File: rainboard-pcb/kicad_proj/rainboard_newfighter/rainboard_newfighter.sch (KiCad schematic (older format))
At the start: 171 parts, among them J1 EJ508A, J2 C46390, J3 Conn_01x03, J4 Conn_01x03, J5 PH2-06-UA, J6 SDS-50J, J7 SDS-50J, J8 PH2-06-UA, J9 PH2-06-UA, Q1 DUAL 30V NMOS, Q2 DUAL 30V NMOS, Q3 30V 10mOhm, U1 RT8298, U2 ATmega16U2-MU, U4 74HC14, U5 ATmega16U2-MU, U6 ATmega2560-16AU, Y3 16MHz

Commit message: Minor schematic and library changes
Identical to previous commit, some files weren't saved.
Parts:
- gave numbers to parts that had none: 17
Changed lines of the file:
@@
 $EndComp
 $Comp
-L lib_symbol:C C?
+L lib_symbol:C C50
 U 1 1 601BBC3A
 P 25600 2900
-F 0 "C?" H 25625 3000 50  0000 L CNN
+F 0 "C50" H 25625 3000 50  0000 L CNN
 F 1 "1uF 25V" V 25450 2700 50  0000 L CNN
 F 2 "Capacitor_SMD:C_0805_2012Metric" H 25638 2750 50  0001 C CNN
@@
 $EndComp
 $Comp
-L lib_symbol:GND #PWR?
+L lib_symbol:GND #PWR0153
 U 1 1 601BBC44
 P 25600 3250
-F 0 "#PWR?" H 25600 3000 50  0001 C CNN
+F 0 "#PWR0153" H 25600 3000 50  0001 C CNN
 F 1 "GND" H 25600 3100 50  0000 C CNN
 F 2 "" H 25600 3250 50  0001 C CNN
@@
 5V_MCU
 $Comp
-L Device:R R?
+L Device:R R21
 U 1 1 605A86DB
 P 16750 5600
-F 0 "R?" H 16820 5646 50  0000 L CNN
+F 0 "R21" H 16820 5646 50  0000 L CNN
 F 1 "19.1k" H 16820 5555 50  0000 L CNN
 F 2 "Resistor_SMD:R_0603_1608Metric" V 16680 5600 50  0001 C CNN
@@
 	16750 6450 16750 6350
 $Comp
-L lib_symbol:GND #PWR?
+L lib_symbol:GND #PWR0154
 U 1 1 605A86E6
 P 16750 6450
-F 0 "#PWR?" H 16750 6200 50  0001 C CNN
+F 0 "#PWR0154" H 16750 6200 50  0001 C CNN
 F 1 "GND" H 16750 6300 50  0000 C CNN
 F 2 "" H 16750 6450 50  0001 C CNN
@@
 $EndComp
 $Comp
-L Device:C C?
+L Device:C C35
 U 1 1 605A86F1
 P 16750 6200
-F 0 "C?" H 16650 6050 50  0000 L CNN
+F 0 "C35" H 16650 6050 50  0000 L CNN
 F 1 "100nf" V 16900 6050 50  0000 L CNN
 F 2 "Capacitor_SMD:C_0603_1608Metric" H 16788 6050 50  0001 C CNN
@@
 	16750 5900 16750 6050
 $Comp
-L Device:C C?
+L Device:C C47
 U 1 1 606525C7
 P 23350 2150
-F 0 "C?" V 23500 1800 50  0000 L CNN
+F 0 "C47" V 23500 1800 50  0000 L CNN
 F 1 "100nf" V 23500 2000 50  0000 L CNN
 F 2 "Capacitor_SMD:C_0603_1608Metric" H 23388 2000 50  0001 C CNN
@@
 	21700 550  21700 8200
 $Comp
-L Device:Resonator Y?
+L Device:Resonator Y2
 U 1 1 60AB98BD
 P 21550 10250
-F 0 "Y?" V 21750 10000 50  0000 C CNN
+F 0 "Y2" V 21750 10000 50  0000 C CNN
 F 1 "16MHz" V 21850 10000 50  0000 C CNN
 F 2 "Crystal:Resonator_SMD_muRata_CSTxExxV-3Pin_3.0x1.1mm" H 21525 10250 50  0001 C CNN
@@
 	21300 10250 21350 10250
 $Comp
-L lib_symbol:GND #PWR?
+L lib_symbol:GND #PWR0157
 U 1 1 60BADC62
 P 16650 4200
-F 0 "#PWR?" H 16650 3950 50  0001 C CNN
+F 0 "#PWR0157" H 16650 3950 50  0001 C CNN
 F 1 "GND" H 16650 4050 50  0000 C CNN
 F 2 "" H 16650 4200 50  0001 C CNN
@@
 $EndComp
 $Comp
-L Device:Resonator Y?
+L Device:Resonator Y1
 U 1 1 60BADC6D
 P 16900 4200
-F 0 "Y?" V 17100 4100 50  0000 C CNN
+F 0 "Y1" V 17100 4100 50  0000 C CNN
 F 1 "16MHz" V 17200 4200 50  0000 C CNN
 F 2 "Crystal:Resonator_SMD_muRata_CSTxExxV-3Pin_3.0x1.1mm" H 16875 4200 50  0001 C CNN
@@
 	16650 4200 16700 4200
 $Comp
-L lib_symbol:C C?
+L lib_symbol:C C48
 U 1 1 60D193CE
 P 24750 9150
-F 0 "C?" H 24775 9250 50  0000 L CNN
+F 0 "C48" H 24775 9250 50  0000 L CNN
 F 1 "1uF 25V" V 24600 8950 50  0000 L CNN
 F 2 "Capacitor_SMD:C_0805_2012Metric" H 24788 9000 50  0001 C CNN
@@
 $EndComp
 $Comp
-L lib_symbol:GND #PWR?
+L lib_symbol:GND #PWR0188
 U 1 1 60D193D8
 P 24750 9500
-F 0 "#PWR?" H 24750 9250 50  0001 C CNN
+F 0 "#PWR0188" H 24750 9250 50  0001 C CNN
 F 1 "GND" H 24750 9350 50  0000 C CNN
 F 2 "" H 24750 9500 50  0001 C CNN
@@
 	24750 9500 24750 9300
 $Comp
-L Device:C C?
+L Device:C C49
 U 1 1 60D193E4
 P 25050 9150
-F 0 "C?" H 25200 9300 50  0000 L CNN
+F 0 "C49" H 25200 9300 50  0000 L CNN
 F 1 "100nf" V 25200 9000 50  0000 L CNN
 F 2 "Capacitor_SMD:C_0603_1608Metric" H 25088 9000 50  0001 C CNN
@@
 $EndComp
 $Comp
-L lib_symbol:GND #PWR?
+L lib_symbol:GND #PWR0189
 U 1 1 60D193EE
 P 25050 9500
-F 0 "#PWR?" H 25050 9250 50  0001 C CNN
+F 0 "#PWR0189" H 25050 9250 50  0001 C CNN
 F 1 "GND" H 25050 9350 50  0000 C CNN
 F 2 "" H 25050 9500 50  0001 C CNN
@@
 5V_USB
 $Comp
-L lib_symbol:C C?
+L lib_symbol:C C45
 U 1 1 60EF9A20
 P 20750 3450
-F 0 "C?" H 20775 3550 50  0000 L CNN
+F 0 "C45" H 20775 3550 50  0000 L CNN
 F 1 "1uF 25V" V 20600 3250 50  0000 L CNN
 F 2 "Capacitor_SMD:C_0805_2012Metric" H 20788 3300 50  0001 C CNN
@@
 $EndComp
 $Comp
-L lib_symbol:GND #PWR?
+L lib_symbol:GND #PWR0190
 U 1 1 60EF9A26
 P 20750 3800
-F 0 "#PWR?" H 20750 3550 50  0001 C CNN
+F 0 "#PWR0190" H 20750 3550 50  0001 C CNN
 F 1 "GND" H 20750 3650 50  0000 C CNN
 F 2 "" H 20750 3800 50  0001 C CNN
@@
 	20750 3800 20750 3600
 $Comp
-L Device:C C?
+L Device:C C46
 U 1 1 60EF9A2E
 P 21050 3450
-F 0 "C?" H 21200 3600 50  0000 L CNN
+F 0 "C46" H 21200 3600 50  0000 L CNN
 F 1 "100nf" V 21200 3300 50  0000 L CNN
 F 2 "Capacitor_SMD:C_0603_1608Metric" H 21088 3300 50  0001 C CNN
@@
 $EndComp
 $Comp
-L lib_symbol:GND #PWR?
+L lib_symbol:GND #PWR0191
 U 1 1 60EF9A34
 P 21050 3800
-F 0 "#PWR?" H 21050 3550 50  0001 C CNN
+F 0 "#PWR0191" H 21050 3550 50  0001 C CNN
 F 1 "GND" H 21050 3650 50  0000 C CNN
 F 2 "" H 21050 3800 50  0001 C CNN
@@
 	21050 3100 21050 3300
 $Comp
-L lib_symbol:C C?
+L lib_symbol:C C39
 U 1 1 60EF9A40
 P 19900 3450
-F 0 "C?" H 19925 3550 50  0000 L CNN
+F 0 "C39" H 19925 3550 50  0000 L CNN
 F 1 "1uF 25V" V 19750 3250 50  0000 L CNN
 F 2 "Capacitor_SMD:C_0805_2012Metric" H 19938 3300 50  0001 C CNN
@@
 $EndComp
 $Comp
-L lib_symbol:GND #PWR?
+L lib_symbol:GND #PWR0192
 U 1 1 60EF9A46
 P 19900 3800
-F 0 "#PWR?" H 19900 3550 50  0001 C CNN
+F 0 "#PWR0192" H 19900 3550 50  0001 C CNN
 F 1 "GND" H 19900 3650 50  0000 C CNN
 F 2 "" H 19900 3800 50  0001 C CNN
@@
 	19900 3800 19900 3600
 $Comp
-L Device:C C?
+L Device:C C41
 U 1 1 60EF9A4E
 P 20200 3450
-F 0 "C?" H 20350 3600 50  0000 L CNN
+F 0 "C41" H 20350 3600 50  0000 L CNN
 F 1 "100nf" V 20350 3300 50  0000 L CNN
 F 2 "Capacitor_SMD:C_0603_1608Metric" H 20238 3300 50  0001 C CNN
@@
 $EndComp
 $Comp
-L lib_symbol:GND #PWR?
+L lib_symbol:GND #PWR0193
 U 1 1 60EF9A54
 P 20200 3800
-F 0 "#PWR?" H 20200 3550 50  0001 C CNN
+F 0 "#PWR0193" H 20200 3550 50  0001 C CNN
 F 1 "GND" H 20200 3650 50  0000 C CNN
 F 2 "" H 20200 3800 50  0001 C CNN
@@
 Connection ~ 4800 10800
 $Comp
-L lib_symbol:C C?
+L lib_symbol:C C17
 U 1 1 6140F8CB
 P 3750 9550
-F 0 "C?" H 3775 9650 50  0000 L CNN
+F 0 "C17" H 3775 9650 50  0000 L CNN
 F 1 "1uF 25V" V 3600 9350 50  0000 L CNN
 F 2 "Capacitor_SMD:C_0805_2012Metric" H 3788 9400 50  0001 C CNN
@@
 $EndComp
 $Comp
-L lib_symbol:GND #PWR?
+L lib_symbol:GND #PWR0194
 U 1 1 6140F8D5
 P 3750 9900
-F 0 "#PWR?" H 3750 9650 50  0001 C CNN
+F 0 "#PWR0194" H 3750 9650 50  0001 C CNN
 F 1 "GND" H 3750 9750 50  0000 C CNN
 F 2 "" H 3750 9900 50  0001 C CNN
@@
 	3750 9200 3750 9400
 $Comp
-L lib_symbol:6N137 U?
+L lib_symbol:6N137 U3
 U 1 1 61517CC3
 P 3650 10600
-F 0 "U?" H 3490 10950 50  0000 C CNN
+F 0 "U3" H 3490 10950 50  0000 C CNN
 F 1 "6N137" H 3650 10250 50  0000 C CNN
 F 2 "" H 3650 10100 50  0001 C CNN
@@
 NONSTANDARD SO-8 PACKAGE
 $Comp
-L lib_symbol:C C?
+L lib_symbol:C C34
 U 1 1 61524583
 P 7350 12500
-F 0 "C?" H 7375 12600 50  0000 L CNN
+F 0 "C34" H 7375 12600 50  0000 L CNN
 F 1 "1uF 25V" V 7200 12300 50  0000 L CNN
 F 2 "Capacitor_SMD:C_0805_2012Metric" H 7388 12350 50  0001 C CNN
@@
 $EndComp
 $Comp
-L lib_symbol:C C?
+L lib_symbol:C C16
 U 1 1 615A0920
 P 1850 9900
-F 0 "C?" H 1875 10000 50  0000 L CNN
+F 0 "C16" H 1875 10000 50  0000 L CNN
 F 1 "DNP-1uF 25V" V 1700 9700 50  0000 L CNN
 F 2 "Capacitor_SMD:C_0805_2012Metric" H 1888 9750 50  0001 C CNN
@@
 $EndComp
 $Comp
-L lib_symbol:C C?
+L lib_symbol:C C4
 U 1 1 616161B4
 P 1500 11300
-F 0 "C?" H 1525 11400 50  0000 L CNN
+F 0 "C4" H 1525 11400 50  0000 L CNN
 F 1 "DNP-1uF 25V" V 1350 11100 50  0000 L CNN
 F 2 "Capacitor_SMD:C_0805_2012Metric" H 1538 11150 50  0001 C CNN
@@
 $EndComp
 $Comp
-L lib_symbol:GND #PWR?
+L lib_symbol:GND #PWR0195
 U 1 1 6168D233
 P 2150 9900
-F 0 "#PWR?" H 2150 9650 50  0001 C CNN
+F 0 "#PWR0195" H 2150 9650 50  0001 C CNN
 F 1 "GND" H 2150 9750 50  0000 C CNN
 F 2 "" H 2150 9900 50  0001 C CNN
@@
 $EndComp
 $Comp
-L lib_symbol:GND #PWR?
+L lib_symbol:GND #PWR0196
 U 1 1 617046B6
 P 1500 11600
-F 0 "#PWR?" H 1500 11350 50  0001 C CNN
+F 0 "#PWR0196" H 1500 11350 50  0001 C CNN
 F 1 "GND" H 1500 11450 50  0000 C CNN
 F 2 "" H 1500 11600 50  0001 C CNN

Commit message: Changes Micro USB to USB B
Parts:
- removed J2: C46390, symbol lib_symbol:USB_B_Micro
- added J2: USB_B, symbol lib_symbol:USB_B
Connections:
- net GND: now also J2.4 (GND)
- net at F2.2: now also J2.1 (VBUS)
- net at R7.2: now also J2.2 (D-)
- net at R6.2: now also J2.3 (D+)
- net at FB1.2: now also J2.5 (Shield)
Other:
- note added: "QUESTION, ASIDE FROM INPUT/OUTPUT CONNECTORS, WHAT ELSE NEEDS ESD PROTECTION?\nEVERY BUTTON/GPIO WOULD BE A LOT, MAYBE BEST TO JUST HAVE THE MCUs/ETC ON THE FAR SIDE SO USER CAN'T REACH MOST INPUTS"
- note added: "USB B Input"
- note removed: "Micro USB Input"
- note removed: "QUESTION, ASIDE FROM INPUT/OUTPUT CONNECTORS, WHAT ELSE NEEDS ESD PROTECTION?\nEVERY BUTTON/GPIO WOULD BE VERY MANY, MAYBE BEST TO JUST HAVE THE MCUs/ETC ON THE FAR SIDE SO USER CAN'T REACH MOST INPUTS"
- note removed: "QUESTION:\nMICRO OK, OR MINI?"
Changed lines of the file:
@@
 VLED
 Text Notes 500  3000 0    250  Italic 50
-Micro USB Input
-$Comp
-L lib_symbol:USB_B_Micro J2
-U 1 1 5FFD55EA
-P 1500 4050
-F 0 "J2" H 1300 4500 50  0000 L CNN
-F 1 "C46390" H 1300 4400 50  0000 L CNN
-F 2 "" H 1650 4000 50  0001 C CNN
-F 3 "~" H 1650 4000 50  0001 C CNN
-	1    1500 4050
-	1    0    0    -1
-$EndComp
+USB B Input
 $Comp
 L lib_symbol:GND #PWR0102
@@
 Wire Wire Line
 	1800 4150 1950 4150
-Text Notes -3600 4400 0    250  ~ 50
-QUESTION:\nMICRO OK, OR MINI?
 Wire Wire Line
 	1950 4150 1950 5200
@@
 MCU2_LED_CTRL
 Text Notes 34400 8350 0    250  ~ 50
-QUESTION, ASIDE FROM INPUT/OUTPUT CONNECTORS, WHAT ELSE NEEDS ESD PROTECTION?\nEVERY BUTTON/GPIO WOULD BE VERY MANY, MAYBE BEST TO JUST HAVE THE MCUs/ETC ON THE FAR SIDE SO USER CAN'T REACH MOST INPUTS
+QUESTION, ASIDE FROM INPUT/OUTPUT CONNECTORS, WHAT ELSE NEEDS ESD PROTECTION?\nEVERY BUTTON/GPIO WOULD BE A LOT, MAYBE BEST TO JUST HAVE THE MCUs/ETC ON THE FAR SIDE SO USER CAN'T REACH MOST INPUTS
 $Comp
 L Device:Resonator Y3
@@
 Wire Wire Line
 	1700 9900 1500 9900
+$Comp
+L lib_symbol:USB_B J2
+U 1 1 60271FDC
+P 1500 4050
+F 0 "J2" H 1350 4400 50  0000 C CNN
+F 1 "USB_B" H 1650 3700 50  0000 C CNN
+F 2 "" H 1650 4000 50  0001 C CNN
+F 3 " ~" H 1650 4000 50  0001 C CNN
+	1    1500 4050
+	1    0    0    -1
+$EndComp
 $EndSCHEMATC

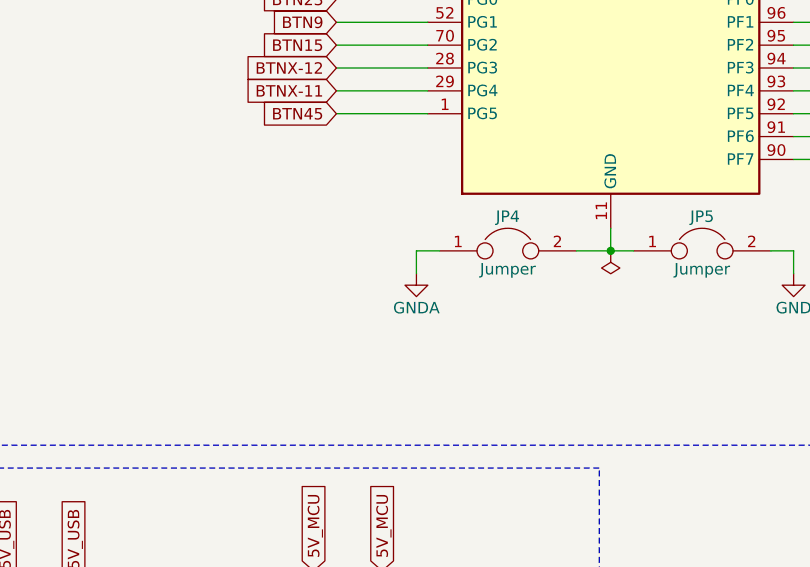
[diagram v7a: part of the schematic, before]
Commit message: adds power flag to GNDA
GNDA was failing ERC check. adds a power flag to fix it
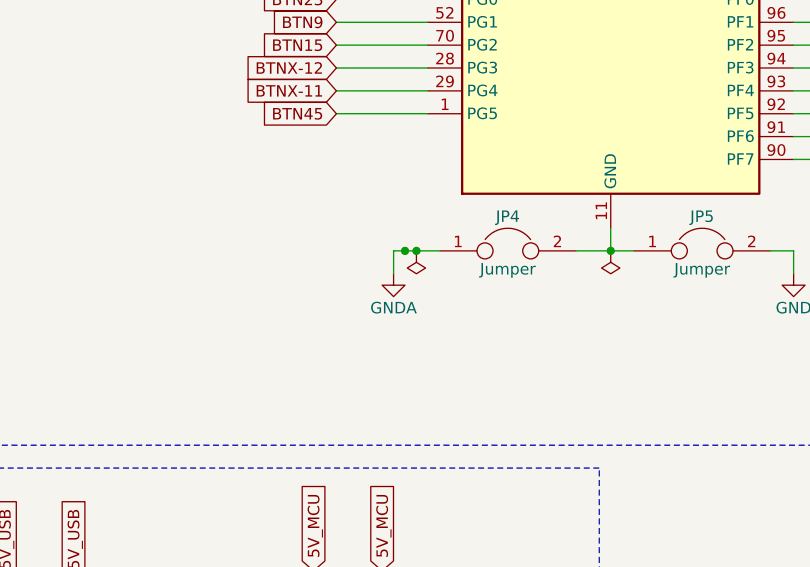
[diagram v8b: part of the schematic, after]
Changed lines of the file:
@@
 $EndComp
 Wire Wire Line
-	26550 7450 26550 7350
-Wire Wire Line
-	26550 7350 26650 7350
+	26450 7450 26450 7350
+Wire Wire Line
+	26450 7350 26500 7350
 Wire Wire Line
 	27400 7350 27250 7350
@@
 L power:GNDA #PWR0179
 U 1 1 608786FC
-P 26550 7450
-F 0 "#PWR0179" H 26550 7200 50  0001 C CNN
-F 1 "GNDA" H 26550 7300 50  0000 C CNN
-F 2 "" H 26550 7450 50  0001 C CNN
-F 3 "" H 26550 7450 50  0001 C CNN
-	1    26550 7450
+P 26450 7450
+F 0 "#PWR0179" H 26450 7200 50  0001 C CNN
+F 1 "GNDA" H 26450 7300 50  0000 C CNN
+F 2 "" H 26450 7450 50  0001 C CNN
+F 3 "" H 26450 7450 50  0001 C CNN
+	1    26450 7450
 	1    0    0    -1
 $EndComp
@@
 	1    0    0    -1
 $EndComp
+$Comp
+L lib_symbol:PWR_FLAG #FLG0109
+U 1 1 6006E1C5
+P 26550 7350
+F 0 "#FLG0109" H 26550 7425 50  0001 C CNN
+F 1 "PWR_FLAG" H 26550 7523 50  0001 C CNN
+F 2 "" H 26550 7350 50  0001 C CNN
+F 3 "~" H 26550 7350 50  0001 C CNN
+	1    26550 7350
+	-1   0    0    1
+$EndComp
+Connection ~ 26500 7350
+Wire Wire Line
+	26500 7350 26550 7350
+Connection ~ 26550 7350
+Wire Wire Line
+	26550 7350 26650 7350
 $EndSCHEMATC
